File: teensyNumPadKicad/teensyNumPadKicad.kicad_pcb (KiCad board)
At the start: 2 copper layers, 82.5 x 125.4 mm, 37 parts, among them U1 Teensy++2.0_(C)

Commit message: Added Gerbers file and ibom.html
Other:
- board text added: "TeensyNumPad"
- board text added: "V1.0"
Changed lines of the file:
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@@
   (general
     (thickness 1.6)
-    (drawings 8)
+    (drawings 10)
     (tracks 328)
     (zones 0)
@@
     (visible_elements 7FFFFFFF)
     (pcbplotparams
-      (layerselection 0x010fc_ffffffff)
-      (usegerberextensions false)
+      (layerselection 0x010f0_ffffffff)
+      (usegerberextensions true)
       (usegerberattributes false)
       (usegerberadvancedattributes false)
@@
       (plotinvisibletext false)
       (padsonsilk false)
-      (subtractmaskfromsilk false)
+      (subtractmaskfromsilk true)
       (outputformat 1)
       (mirror false)
-      (drillshape 1)
+      (drillshape 0)
       (scaleselection 1)
-      (outputdirectory ""))
+      (outputdirectory "C:/Dev/TeensyNumPad/TeensyNumPad/gerberFiles"))
   )
   (net 0 "")
@@
     )
   )
+  (gr_text V1.0 (at 147.6375 66.675 90) (layer F.SilkS)
+    (effects (font (size 2 2) (thickness 0.5)))
+  )
+  (gr_text TeensyNumPad (at 143.66875 66.675 90) (layer F.SilkS)
+    (effects (font (size 2 2) (thickness 0.5)))
+  )
   (gr_line (start 71.4375 177.8) (end 147.6375 177.8) (layer Edge.Cuts) (width 0.05))

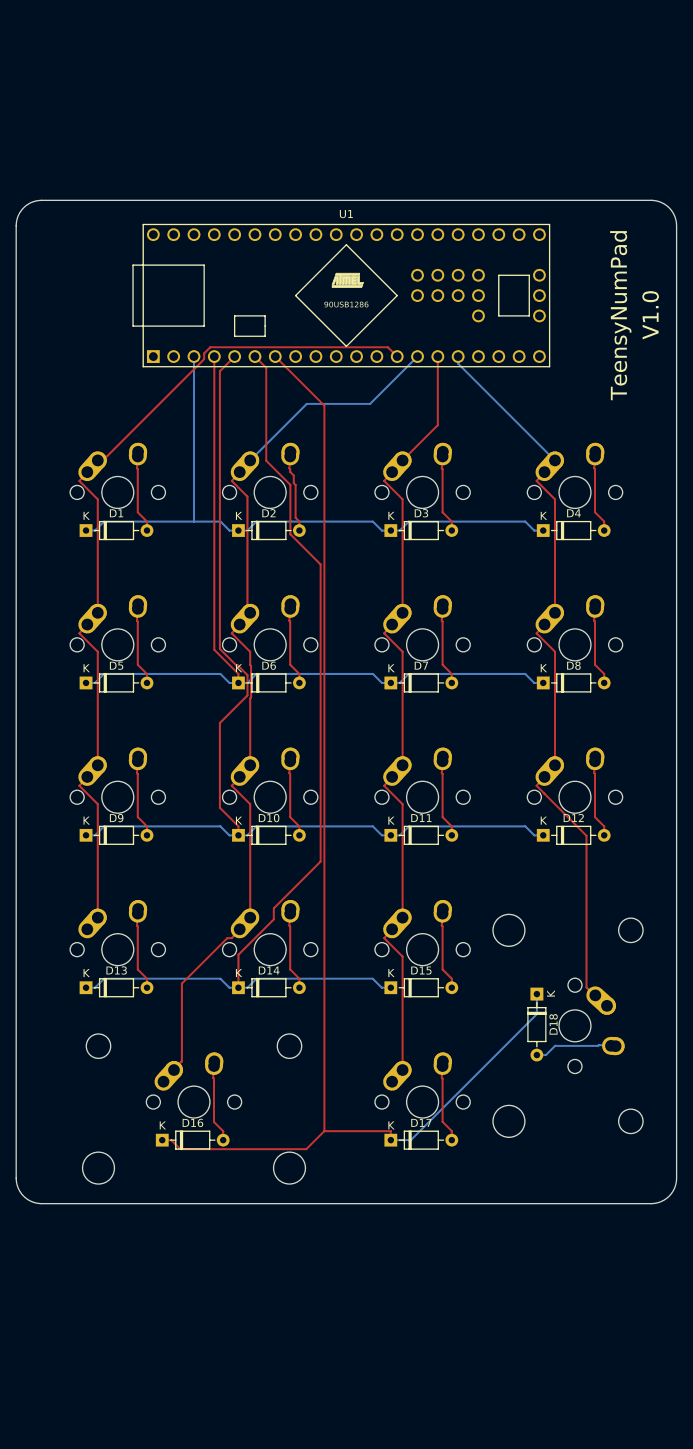
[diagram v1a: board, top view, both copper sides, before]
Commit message: Add 5 pin din plug for connection to an Amiga
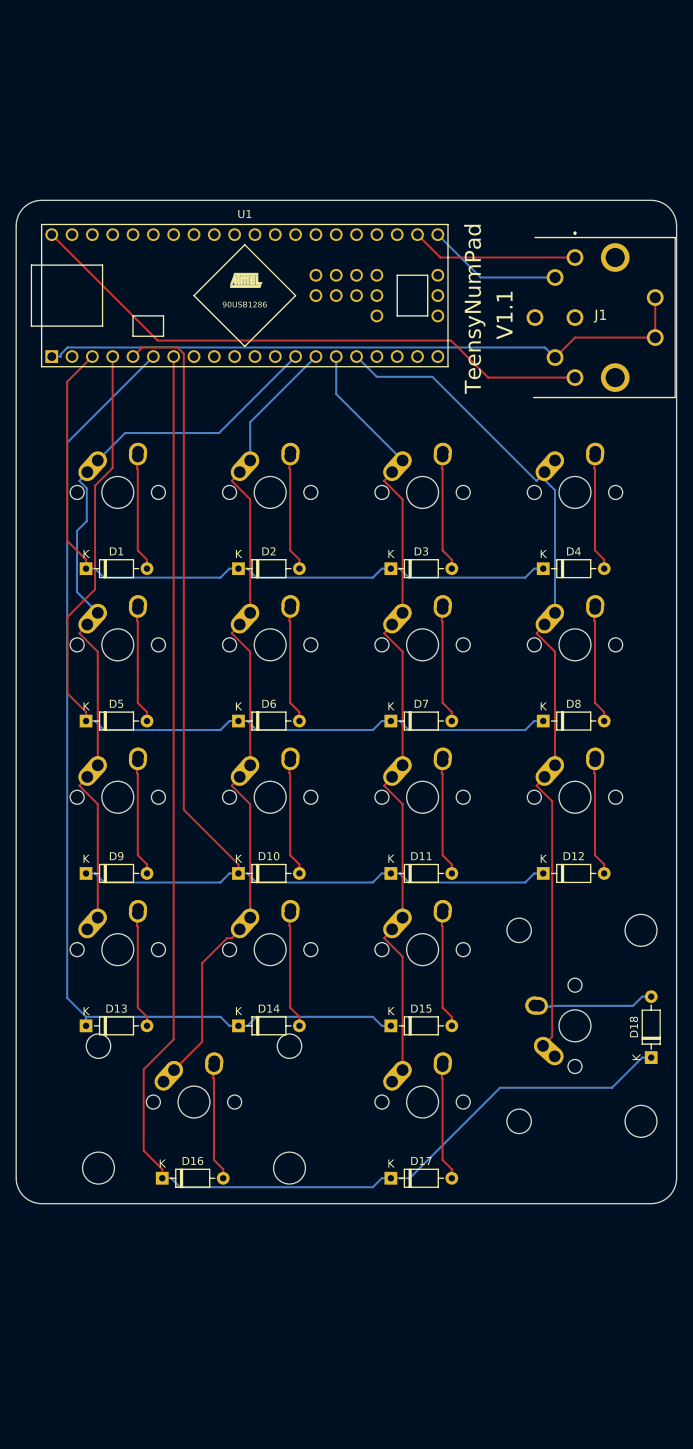
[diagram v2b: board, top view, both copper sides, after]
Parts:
- added J1: 61PC6F, SamacSys_Parts:61PC6F, F.Cu at (138.1, 59.5)
- moved D18 16.3 mm to (147.6, 159.5), turned to 90 degrees
- moved U1 12.7 mm to (96.8, 64.3)
- moved D10 4.76 mm to (96.0, 136.5)
- moved D11 4.76 mm to (115.1, 136.5)
- moved D12 4.76 mm to (134.1, 136.5)
- moved D16 4.76 mm to (86.5, 174.6)
- moved D17 4.76 mm to (115.1, 174.6)
- moved D9 4.76 mm to (77.0, 136.5)
- moved D5 4.76 mm to (77.0, 117.5)
- moved D6 4.76 mm to (96.0, 117.5)
- moved D7 4.76 mm to (115.1, 117.5)
- moved D8 4.76 mm to (134.1, 117.5)
- moved D13 4.76 mm to (77.0, 155.6)
- moved D14 4.76 mm to (96.0, 155.6)
- moved D15 4.76 mm to (115.1, 155.6)
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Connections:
- U1 pad 1: Net-(U1-Pad1) -> GND
- U1 pad 43: Net-(U1-Pad43) -> VCC
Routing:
- net GND: track 0.00 -> 82.6 mm
- net VCC: track 0.00 -> 72.8 mm
- net Net-(J1-Pad1): track 0.00 -> 20.9 mm
- net Net-(J1-Pad2): track 0.00 -> 16.9 mm
- net COL3: track 94.6 -> 110.4 mm
- net ROW4: track 157.8 -> 173.5 mm
- net COL0: track 109.0 -> 95.9 mm
- net COL1: track 115.9 -> 104.5 mm
- net ROW2: track 124.5 -> 134.9 mm
- net ROW0: track 80.6 -> 88.7 mm
- net ROW1: track 102.0 -> 108.8 mm
- net Net-(D18-Pad2): track 10.4 -> 15.1 mm
- net Net-(D17-Pad2): track 10.4 -> 15.1 mm
- net Net-(D16-Pad2): track 10.4 -> 15.1 mm
- net Net-(D9-Pad2): track 10.4 -> 15.1 mm
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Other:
- net class Default: trace_width 0.25 -> 0.254
- net class Power added: clearance 0.2, trace_width 0.381, via_dia 0.8, via_drill 0.4
- board text added: "V1.1"
- board text removed: "V1.0"

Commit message: Add Modifier keys + LEDs
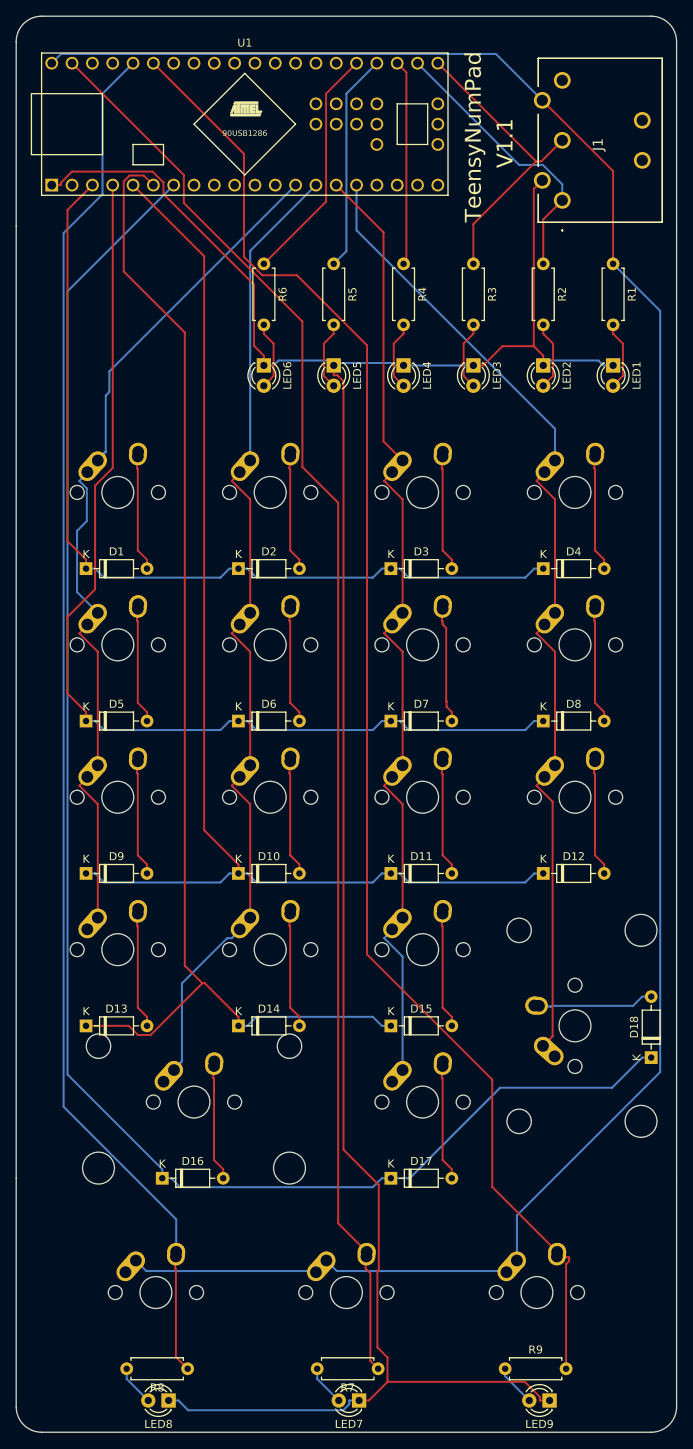
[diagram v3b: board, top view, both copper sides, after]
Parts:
- added LED1: LED, LED_THT:LED_D3.0mm, F.Cu at (142.9, 73.0)
- added LED2: LED, LED_THT:LED_D3.0mm, F.Cu at (134.1, 73.0)
- added LED3: LED, LED_THT:LED_D3.0mm, F.Cu at (125.4, 73.0)
- added LED4: LED, LED_THT:LED_D3.0mm, F.Cu at (116.7, 73.0)
- added LED5: LED, LED_THT:LED_D3.0mm, F.Cu at (108.0, 73.0)
- added LED6: LED, LED_THT:LED_D3.0mm, F.Cu at (99.2, 73.0)
- added LED7: LED, LED_THT:LED_D3.0mm, F.Cu at (111.1, 202.4)
- added LED8: LED, LED_THT:LED_D3.0mm, F.Cu at (87.3, 202.4)
- added LED9: LED, LED_THT:LED_D3.0mm, F.Cu at (134.9, 202.4)
- added MX19: MX-NoLED, MX_Alps_Hybrid:MX-1.25U-NoLED, F.Cu at (109.5, 188.9)
- added MX20: MX-NoLED, MX_Alps_Hybrid:MX-1.25U-NoLED, F.Cu at (85.7, 188.9)
- added MX21: MX-NoLED, MX_Alps_Hybrid:MX-1.25U-NoLED, F.Cu at (133.3, 188.9)
- added R1: 150, Resistor_THT:R_Axial_DIN0207_L6.3mm_D2.5mm_P7.62mm_Horizontal, F.Cu at (142.9, 60.3)
- added R2: 150, Resistor_THT:R_Axial_DIN0207_L6.3mm_D2.5mm_P7.62mm_Horizontal, F.Cu at (134.1, 60.3)
- added R3: 150, Resistor_THT:R_Axial_DIN0207_L6.3mm_D2.5mm_P7.62mm_Horizontal, F.Cu at (125.4, 60.3)
- added R4: 150, Resistor_THT:R_Axial_DIN0207_L6.3mm_D2.5mm_P7.62mm_Horizontal, F.Cu at (116.7, 60.3)
- added R5: 150, Resistor_THT:R_Axial_DIN0207_L6.3mm_D2.5mm_P7.62mm_Horizontal, F.Cu at (108.0, 60.3)
- added R6: 150, Resistor_THT:R_Axial_DIN0207_L6.3mm_D2.5mm_P7.62mm_Horizontal, F.Cu at (99.2, 60.3)
- added R7: 150, Resistor_THT:R_Axial_DIN0207_L6.3mm_D2.5mm_P7.62mm_Horizontal, F.Cu at (113.5, 198.4)
- added R8: 150, Resistor_THT:R_Axial_DIN0207_L6.3mm_D2.5mm_P7.62mm_Horizontal, F.Cu at (89.7, 198.4)
- added R9: 150, Resistor_THT:R_Axial_DIN0207_L6.3mm_D2.5mm_P7.62mm_Horizontal, F.Cu at (129.4, 198.4)
- J1: value 61PC6F -> KCDX-5S-S2; footprint SamacSys_Parts:61PC6F -> SamacSys_Parts:KCDX5SS2
- moved U1 21.4 mm to (96.8, 42.9)
- moved J1 7.32 mm to (136.5, 52.4), turned to 270 degrees
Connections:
- net Net-(J1-Pad1) renamed KCLK
- net Net-(J1-Pad2) renamed KDAT
- U1 pad 26: Net-(U1-Pad26) -> STA1
- U1 pad 27: Net-(U1-Pad27) -> STA2
- U1 pad 28: Net-(U1-Pad28) -> STA3
- U1 pad 38: Net-(U1-Pad38) -> RAMI
- U1 pad 39: Net-(U1-Pad39) -> CTRL
- U1 pad 42: Net-(U1-Pad42) -> LAMI
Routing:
- net GND: track 82.6 -> 294.2 mm
- net VCC: track 72.8 -> 274.8 mm
- net RAMI: track 0.00 -> 188.2 mm
- net LAMI: track 0.00 -> 179.1 mm
- net CTRL: track 0.00 -> 173.3 mm
- net STA3: track 0.00 -> 29.9 mm
- net ROW4: track 173.5 -> 202.8 mm
- net STA2: track 0.00 -> 27.3 mm
- net STA1: track 0.00 -> 25.7 mm
- net ROW3: track 128.6 -> 153.9 mm
- net COL1: track 104.5 -> 127.3 mm
- net ROW1: track 108.8 -> 130.2 mm
- net COL2: track 102.1 -> 123.6 mm
- net ROW0: track 88.7 -> 110.1 mm
- net KDAT: track 16.9 -> 37.8 mm
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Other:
- board size 82.5 x 125.4 mm -> 82.6 x 177 mm

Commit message: Create new gerber files
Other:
- board text added: "V1.2"
- board text removed: "V1.1"
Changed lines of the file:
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@@
   (gr_line (start 150.8125 32.54375) (end 150.8125 55.5625) (layer Edge.Cuts) (width 0.05))
   (gr_line (start 68.2625 32.54375) (end 68.2625 55.5625) (layer Edge.Cuts) (width 0.05))
-  (gr_text V1.1 (at 129.38125 45.24375 90) (layer F.SilkS)
+  (gr_text V1.2 (at 129.38125 45.24375 90) (layer F.SilkS)
     (effects (font (size 2 2) (thickness 0.5)))
   )

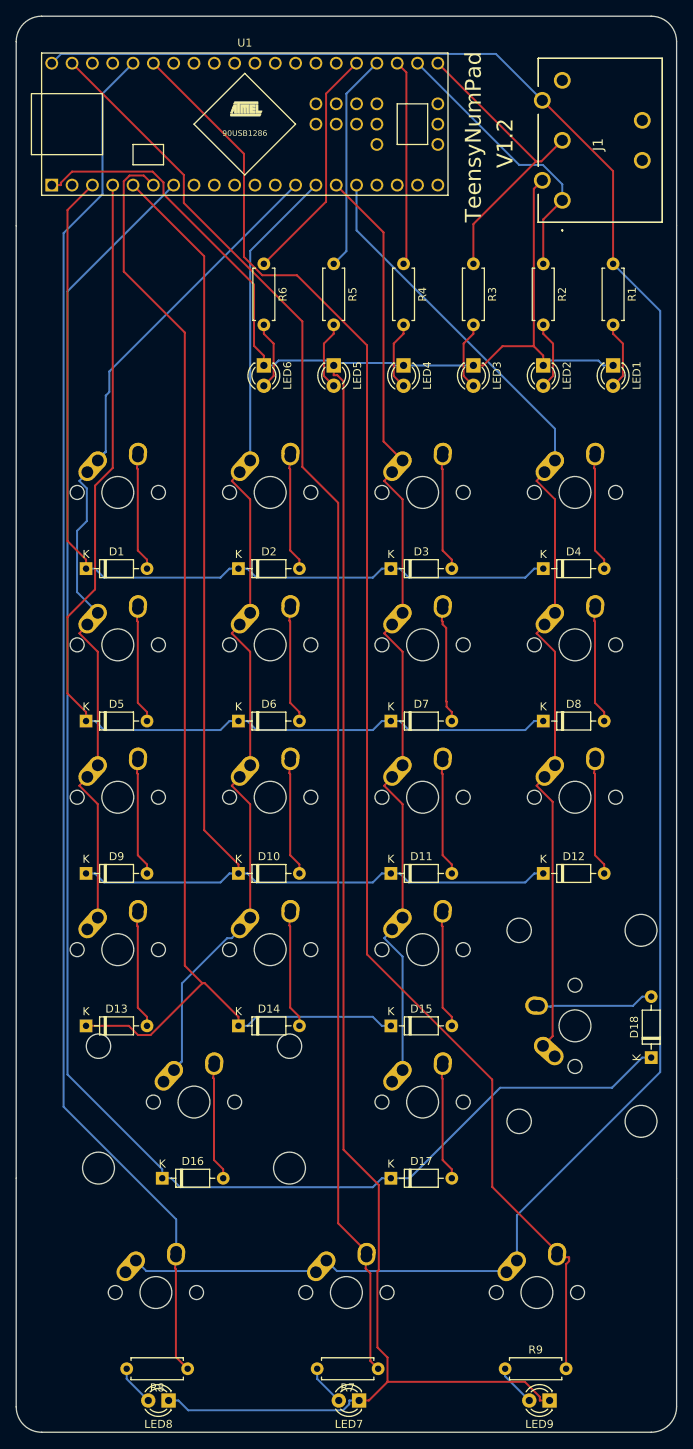
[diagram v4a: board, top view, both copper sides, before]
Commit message: Move diodes for 2u keys
Diode was clashing with stabilizer
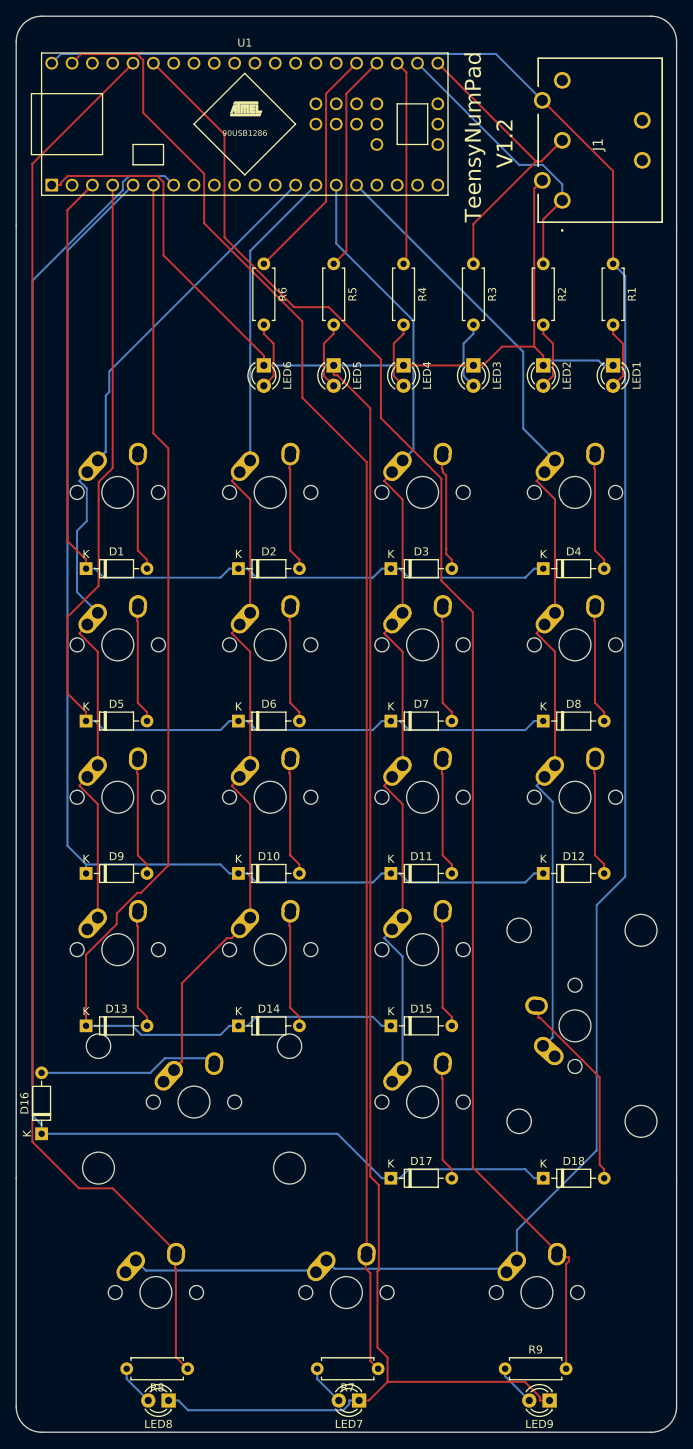
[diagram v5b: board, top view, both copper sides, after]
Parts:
- moved D18 20.2 mm to (134.1, 174.6), turned to 0 degrees
- moved D16 16.1 mm to (71.4, 169.1), turned to 90 degrees
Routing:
- net Net-(D18-Pad2): track 15.1 -> 25.7 mm
- net Net-(D16-Pad2): track 15.1 -> 23.1 mm
- net LAMI: track 179.1 -> 185.5 mm
- net CTRL: track 173.3 -> 179.0 mm
- net ROW4: track 202.8 -> 197.2 mm
- net ROW3: track 153.9 -> 150.3 mm
- net VCC: track 274.8 -> 271.5 mm
- net ROW2: track 151.4 -> 149.9 mm
- net GND: track 294.2 -> 292.8 mm
- net COL2: track 123.6 -> 124.7 mm

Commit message: Updated Schema and PCB
Fixed pin assignments on 5 pin DIN socket as follows:
1      Not Connected
2      KDAT
3      KCLK
4      +5V
5      GND
This is because the pins are numbered from right to left rather than left to right.  Also increased the size of the resistor footprints.
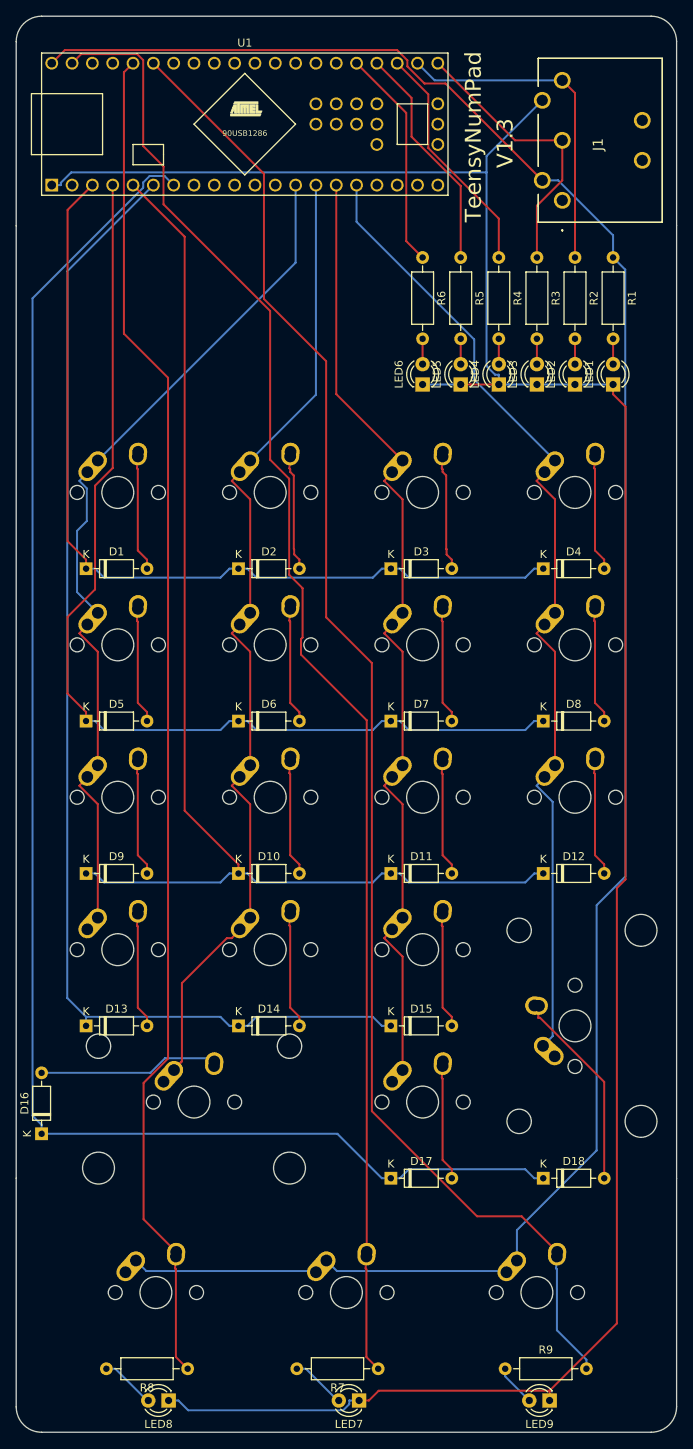
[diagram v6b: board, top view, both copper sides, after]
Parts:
- R1, R2, R3, R4, R5, R6, R7, R8, R9: footprint Resistor_THT:R_Axial_DIN0207_L6.3mm_D2.5mm_P7.62mm_Horizontal -> Resistor_THT:R_Axial_DIN0207_L6.3mm_D2.5mm_P10.16mm_Horizontal
- moved LED6 20.0 mm to (119.1, 75.4), turned to 90 degrees
- moved R6 19.9 mm to (119.1, 59.5)
- moved LED5 16.1 mm to (123.8, 75.4), turned to 90 degrees
- moved R5 15.9 mm to (123.8, 59.5)
- moved LED4 12.1 mm to (128.6, 75.4), turned to 90 degrees
- moved R4 11.9 mm to (128.6, 59.5)
- moved LED3 8.29 mm to (133.3, 75.4), turned to 90 degrees
- moved R3 7.98 mm to (133.3, 59.5)
- moved LED2 4.63 mm to (138.1, 75.4), turned to 90 degrees
- moved R2 4.05 mm to (138.1, 59.5)
- moved LED1 2.38 mm to (142.9, 75.4), turned to 90 degrees
- moved R1 0.79 mm to (142.9, 59.5)
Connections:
- J1 pad 1: KCLK -> Net-(J1-Pad1)
- J1 pad 3: Net-(J1-Pad3) -> KCLK
- J1 pad 4: GND -> VCC
- J1 pad 5: VCC -> GND
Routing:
- net CTRL: track 179.0 -> 169.6 mm
- net GND: track 292.8 -> 299.3 mm
- net KCLK: track 35.3 -> 41.8 mm
- net Net-(LED5-Pad2): track 8.64 -> 3.18 mm
- net Net-(LED3-Pad2): track 8.64 -> 3.18 mm
- net Net-(LED2-Pad2): track 8.64 -> 3.18 mm
- net Net-(LED1-Pad2): track 8.64 -> 3.18 mm
- net Net-(LED6-Pad2): track 8.64 -> 3.18 mm
- net Net-(LED4-Pad2): track 8.64 -> 3.18 mm
- net VCC: track 271.5 -> 267.4 mm
- net STA1: track 25.7 -> 29.5 mm
- net KDAT: track 37.8 -> 35.5 mm
- net STA3: track 29.9 -> 27.7 mm
- net Net-(LED7-Pad2): track 5.09 -> 6.88 mm
- net Net-(LED8-Pad2): track 5.09 -> 6.88 mm
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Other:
- board text added: "V1.3"
- board text removed: "V1.2"
